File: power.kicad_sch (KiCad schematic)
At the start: 33 parts, among them J17 Conn_02x08_Odd_Even, J18 Conn_Coaxial, U11 TLV1117-33

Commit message: redoing file add
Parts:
- renumbered C31 to C42, C32 to C43, C33 to C44, C34 to C45, C35 to C46, C36 to C47, C37 to C48, C38 to C49, C39 to C50, C40 to C51, C41 to C52, C42 to C53, C43 to C54, C44 to C55, C45 to C56, C46 to C57, C47 to C58, C48 to C59, C49 to C60, C50 to C61, C51 to C62, C52 to C63, C53 to C64, C54 to C65, J17 to J18, J18 to J19, R52 to R56, R53 to R57, U11 to U12

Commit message: WIP layout
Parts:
- removed C51, C52, C57, C58: C_Polarized_Small, Capacitor_THT:CP_Radial_D8.0mm_P3.50mm, symbol Device:C_Polarized_Small
- removed C53, C54, C55, C56, C60, C61, C63, C64: C_Small, Capacitor_SMD:C_0603_1608Metric, symbol Device:C_Small
- removed L3, L4: L_Ferrite_Small, Inductor_SMD:L_0603_1608Metric, symbol Device:L_Ferrite_Small
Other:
- moved on the sheet: J18

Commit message: WIP layout
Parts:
- J18: footprint Connector_PinHeader_2.54mm:PinHeader_2x08_P2.54mm_Vertical -> Connector_PinSocket_2.54mm:PinSocket_2x08_P2.54mm_Vertical
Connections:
- net +3.3V renamed VDD
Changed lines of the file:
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@@
 			"AAAAAAAAAAAAAAAAAAAAAAAAAAAAAAAAAAAAAAAAAAAAAAAAAAAAAAAAAAAAAAAAAAAAAAAAAAAA"
 			"AAAAAAAAAAAAAAAAAAAAAAAAAAAAAAAAAAAAAAAAAAAAAAAAAAAAAAAAAAAAAAAAAAAAAAAAAAAA"
-			"AAAAAAAAAAAAAAAAAAAAAAAAAAAAAAAAAAAAAAAAAAAAAAAAAAAAAA=="
+			"AAAAAAAAAAAAAAAAAAAAAAAAAAAAAAAAAAAAAAAAAAAAAAAAAAAAAN1Ov5bOFj9lap+6KWdivzr6"
+			"7j4jJ746oHVlv4gE4z5OfZi6kRgxQa2W6sBeFIk+8KYwQUn/68C5bEc/N5MwQWlK7MBeFIk+llha"
+			"vwilBT+te666AAAAAAAAAAAAAAAAAAAAAAAAAAAAAAAA////////////////GbEcv6iSzDpU5XhB"
+			"AAAAAHpb+j8AAAAAT2eWwXYxz787XwAA8AAAAAAAAAAgAAAAAAAAAPtw4o8+XwAAsLVVfDtfAAAA"
+			"AAAAAAAAAHFvGAAAAAAAkCZufDtfAAAgGz8E/HkAAAAAAAAAAAAAAAAAAAAAAADWWDtBDcjuwHT7"
+			"BT8FAAAA4KHvc/t5AADAYO94O18AAAAAAADoino/GUxSPpqzFrtnQn0/RGsVPieJDjveIXM/okeg"
+			"PjnBCDt0ZjtBPRLvwF4UiT5rdjtBCL/vwLlsRz9BOztBEtHtwLlsRz+79Hg/l4xuPkj+DzsAAAAA"
+			"AAAAAAAAAAAAAAAAAAAAAAAAAAD///////////////96THU+RhEUO3PGHkEAAAAAk8eiP6mshMGp"
+			"rIRBzycvPztfAADwAAAAAAAAACAAAAAAAAAA63Pijz5fAADAtlV8O18AAAAAAAAAAAAAYW4YAAAA"
+			"AACQJm58O18AACAbPwT8eQAAAAAAAAAAAAAAAAAAAAAAACp1MEEu6OzAdPsFPwUAAADgoe9z+3kA"
+			"AMBg73g7XwAAAAAAAKJ1Zb+GBOM+TX2YuilnYr86+u4+Iye+Ot4vc7/38p8+HNbQOjeTMEFpSuzA"
+			"XhSJPvCmMEFJ/+vAuWxHP2VDMEES0e3AuWxHPxpma793Osk+uxXTOgAAAAAAAAAAAAAAAAAAAAAA"
+			"AAAAAAAAAP///////////////8/W2r7mjuW6tRBjQQAAAABe+tE/N7OMQTezjMFxhKE+O18AAPAA"
+			"AAAAAAAAIAAAAAAAAACbcuKPPl8AANC3VXw7XwAAAAAAAAAAAABRbRgAAAAAAJAmbnw7XwAAIBs/"
+			"BPx5AAAAAAAAAAAAAAAAAAAAAAAAFm0xQSrW6cB0+wU/BQAAAOCh73P7eQAAwGDveDtfAAAAAAAA"
+			"wVcyvxaoNz81BaW6v+NKv0UdHD9ApK86dt1Ov5bOFj9lap+6msExQacV6cBeFIk+7DExQfFU6sC5"
+			"bEc/kRgxQa2W6sBeFIk+SV5Av8PoKD8UyKS6AAAAAAAAAAAAAAAAAAAAAAAAAAAAAAAA////////"
+			"////////+Mdgv8FJ2zr4C4xBAAAAAHtb+j8AAAAAiDaqwUGdz787XwAA8AAAAAAAAAAgAAAAAAAA"
+			"AIt94o8+XwAA4LhVfDtfAAAAAAAAAAAAAEFsGAAAAAAAkCZufDtfAA=="
 		)
 	)
@@
 			"AAAAZQAAAHoAAAA3AAAAZgAAAGgAAAB6AAAASAAAAFUAAAAzAAAAWgAAAFQAAABGAAAATQAAAFUA"
 			"AAB3AAAARAAAAEUAAABVAAAAWgAAAFUAAAAxAAAAdAAAAG0AAAA5AAAAQQAAAEUAAABsAAAAdgAA"
+			"AHoAAAA1AAAAUwAAAFUAAABrAAAAWgAAADMAAABTAAAAUAAAAFUAAABRAAAAQwAAAEsAAABFAAAA"
+			"WAAAAHgAAAAxAAAAMAAAAHcAAABCAAAAWQAAAHgAAABRAAAAcwAAAGsAAAA3AAAAaAAAAFkAAABC"
+			"AAAAawAAAFQAAABoAAAASgAAAEMAAABpAAAAVQAAAEkAAABJAAAAeAAAAHAAAABKAAAAWQAAADMA"
+			"AABpAAAAYQAAAEwAAABqAAAANAAAACsAAABOAAAAMgAAAHUAAAArAAAATgAAADUAAABYAAAAaAAA"
+			"AHgAAABIAAAAWQAAADYAAABYAAAAWgAAAHQAAABqAAAAMAAAADMAAABOAAAANQAAAGYAAABQAAAA"
+			"NQAAAHgAAABWAAAARgAAAFMAAABjAAAAUgAAAE8AAABKAAAAMwAAAGwAAABiAAAAZgAAAE4AAAAv"
+			"AAAAZgAAADIAAABuAAAAcgAAAFEAAAA2AAAAYgAAAFMAAABuAAAANwAAAEoAAABuAAAAUAAAAEYA"
+			"AAAxAAAAWgAAAFgAAABWAAAAOQAAAFEAAABKAAAAegAAAFcAAABqAAAAUwAAAE8AAAA0AAAAWQAA"
+			"AHgAAABUAAAAbgAAAHEAAABJAAAAUQAAAFIAAAA5AAAARwAAAHYAAABwAAAATQAAADEAAABZAAAA"
+			"SQAAAFgAAABuAAAAeAAAAGQAAAB2AAAAYgAAADgAAABmAAAAVwAAAGIAAAA3AAAATQAAAE8AAABQ"
+			"AAAANQAAAGYAAAAzAAAANwAAAHUAAABOAAAAOQAAAFIAAABMAAAAbAAAAC8AAABTAAAAZgAAAHYA"
+			"AABFAAAATAAAAGUAAAB2AAAAVQAAAHEAAABBAAAASQAAAGcAAABnAAAAagAAAEIAAABzAAAATgAA"
+			"AGQAAAB1AAAAMgAAAGEAAAArAAAATwAAAFgAAABmAAAAeQAAAGQAAAB1AAAAMwAAAGsAAAAwAAAA"
+			"dAAAAEgAAABBAAAATwAAAGoAAABNAAAARwAAAGYAAAB5AAAAegAAAG4AAAA1AAAARwAAAHIAAABW"
+			"AAAANQAAAFcAAABsAAAASgAAAGIAAABTAAAALwAAAHgAAAAvAAAALwAAAGIAAAAvAAAAOAAAAEcA"
+			"AAAvAAAAKwAAAGgAAABxAAAAWgAAAEQAAABuAAAAcgAAADcAAABiAAAAVgAAAGsAAABvAAAAUAAA"
+			"AEYAAABUAAAAMwAAAHYAAABzAAAAOQAAADIAAABkAAAAOQAAAG0AAABuAAAAbgAAADQAAAByAAAA"
+			"LwAAADgAAABTAAAAcwAAAGcAAABXAAAAUAAAAHoAAABKAAAAZgAAADYAAABCAAAAdgAAAGEAAABZ"
 			"AA=="
 		)
@@
 	)
 	(symbol
-		(lib_id "power:+3.3V")
-		(at 226.06 55.88 0)
-		(unit 1)
-		(exclude_from_sim no)
-		(in_bom yes)
-		(on_board yes)
-		(dnp no)
-		(fields_autoplaced yes)
-		(property "Reference" "#PWR099"
-			(at 226.06 59.69 0)
-			(effects
-				(font
-					(size 1.27 1.27)
-				)
-				(hide yes)
-			)
-		)
-		(property "Value" "+3.3V"
-			(at 226.06 51.7469 0)
-			(effects
-				(font
-					(size 1.27 1.27)
-				)
-			)
-		)
-		(property "Footprint" ""
-			(at 226.06 55.88 0)
-			(effects
-				(font
-					(size 1.27 1.27)
-				)
-				(hide yes)
-			)
-		)
-		(property "Datasheet" ""
-			(at 226.06 55.88 0)
-			(effects
-				(font
-					(size 1.27 1.27)
-				)
-				(hide yes)
-			)
-		)
-		(property "Description" "Power symbol creates a global label with name \"+3.3V\""
-			(at 226.06 55.88 0)
-			(effects
-				(font
-					(size 1.27 1.27)
-				)
-				(hide yes)
-			)
-		)
-		(pin "1"
-		)
-		(instances
-			(project ""
-				(path "/afe1fbe1-30b6-4eb7-94cf-5d2700d51271/1ed0643a-d8c6-437c-9189-4d518e5ee62a"
-					(reference "#PWR099")
-					(unit 1)
-				)
-			)
-		)
-	)
-	(symbol
 		(lib_id "power:GND")
 		(at 60.96 72.39 270)
@@
 			)
 		)
-		(property "Footprint" "Connector_PinHeader_2.54mm:PinHeader_2x08_P2.54mm_Vertical"
+		(property "Footprint" "Connector_PinSocket_2.54mm:PinSocket_2x08_P2.54mm_Vertical"
 			(at 68.58 69.85 0)
 			(effects
@@
 	)
 	(symbol
+		(lib_id "power:VDD")
+		(at 226.06 55.88 0)
+		(unit 1)
+		(exclude_from_sim no)
+		(in_bom yes)
+		(on_board yes)
+		(dnp no)
+		(fields_autoplaced yes)
+		(property "Reference" "#PWR073"
+			(at 226.06 59.69 0)
+			(effects
+				(font
+					(size 1.27 1.27)
+				)
+				(hide yes)
+			)
+		)
+		(property "Value" "VDD"
+			(at 226.06 51.7469 0)
+			(effects
+				(font
+					(size 1.27 1.27)
+				)
+			)
+		)
+		(property "Footprint" ""
+			(at 226.06 55.88 0)
+			(effects
+				(font
+					(size 1.27 1.27)
+				)
+				(hide yes)
+			)
+		)
+		(property "Datasheet" ""
+			(at 226.06 55.88 0)
+			(effects
+				(font
+					(size 1.27 1.27)
+				)
+				(hide yes)
+			)
+		)
+		(property "Description" "Power symbol creates a global label with name \"VDD\""
+			(at 226.06 55.88 0)
+			(effects
+				(font
+					(size 1.27 1.27)
+				)
+				(hide yes)
+			)
+		)
+		(pin "1"
+		)
+		(instances
+			(project "pcm3168a_euro1"
+				(path "/afe1fbe1-30b6-4eb7-94cf-5d2700d51271/1ed0643a-d8c6-437c-9189-4d518e5ee62a"
+					(reference "#PWR073")
+					(unit 1)
+				)
+			)
+		)
+	)
+	(symbol
 		(lib_id "power:GND")
 		(at 73.66 69.85 90)
@@
 		(on_board yes)
 		(dnp no)
-		(fields_autoplaced yes)
 		(property "Reference" "C42"
 			(at 132.969 41.4217 0)
@@
 		)
 		(property "Value" "C_Polarized_Small"
-			(at 132.969 43.846 0)
+			(at 114.046 49.784 0)
 			(effects
 				(font

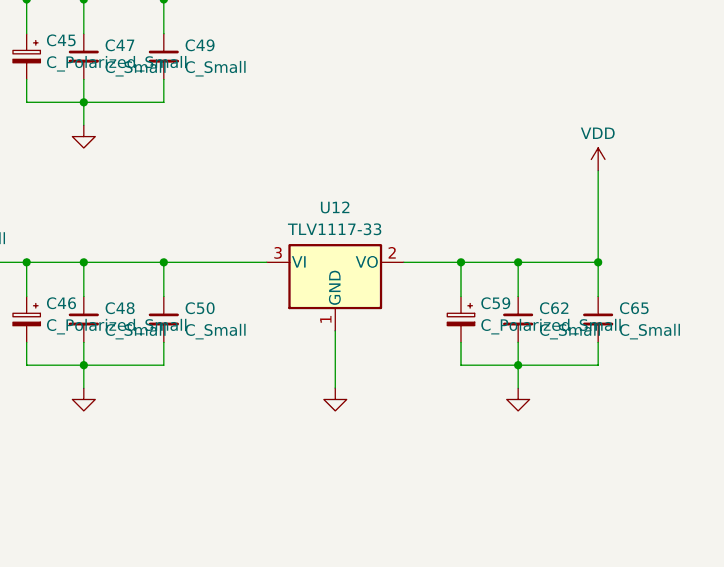
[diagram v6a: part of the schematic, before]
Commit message: WIP: layout mostly done, everything connected and looking good. still have TODO list + DRC
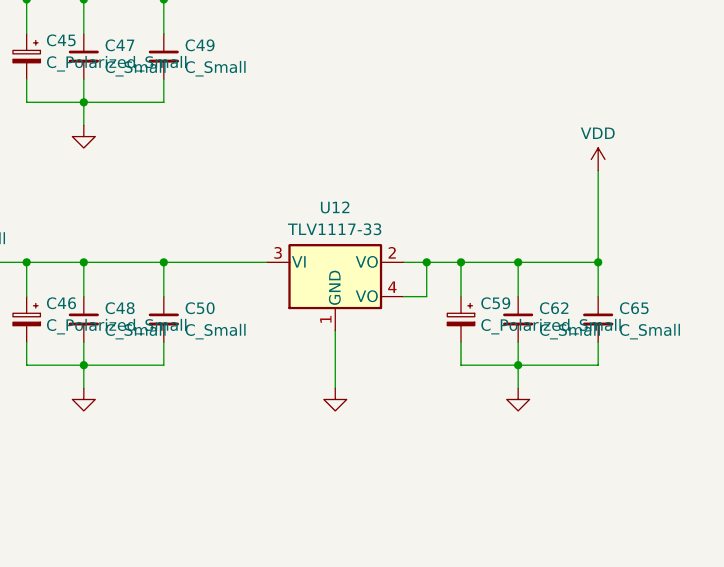
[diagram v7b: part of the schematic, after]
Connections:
- net VDD: now also U12.4 (VO)
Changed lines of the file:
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@@
 	)
 	(junction
+		(at 207.01 66.04)
+		(diameter 0)
+		(color 0 0 0 0)
+	)
+	(junction
 		(at 168.91 36.83)
 		(diameter 0)
@@
 	(wire
 		(pts
+			(xy 204.47 69.85) (xy 207.01 69.85)
+		)
+		(stroke
+			(width 0)
+			(type default)
+		)
+	)
+	(wire
+		(pts
 			(xy 146.05 48.26) (xy 146.05 45.72)
 		)
@@
 	(wire
 		(pts
+			(xy 207.01 66.04) (xy 210.82 66.04)
+		)
+		(stroke
+			(width 0)
+			(type default)
+		)
+	)
+	(wire
+		(pts
 			(xy 210.82 77.47) (xy 217.17 77.47)
 		)
@@
 	(wire
 		(pts
+			(xy 207.01 69.85) (xy 207.01 66.04)
+		)
+		(stroke
+			(width 0)
+			(type default)
+		)
+	)
+	(wire
+		(pts
 			(xy 60.96 67.31) (xy 57.15 67.31)
 		)
@@
 	(wire
 		(pts
-			(xy 204.47 66.04) (xy 210.82 66.04)
+			(xy 204.47 66.04) (xy 207.01 66.04)
 		)
 		(stroke
@@
 			"8cCa12QAAAsU50CqpavA8DJzPaXC80DgDanAa3l+PVhr7UDEWarALtZ4PQIAAACYdeDP0WQAAAAA"
 			"AAAAAAAAAAAAAAAAAACAZCrMXHAAAGTN5j4YN6o+AAAAANFkAADAAAAAAAAAAIFbAAAAAAAAkPG9"
-			"29FkAAAgG/+8XXAAAAAAAAAAAAAAAAAAAAAAAABo8cCa12QAAJ0z5g=="
+			"29FkAAAgG/+8XXAAAAAAAAAAAAAAAAAAAAAAAABo8cCa12QAAJ0z5gAAAAAAAAAAAAAAAAAAAAAA"
+			"AAAAAAAAAAAAAAAAAAAAAAAAAAAAAAAAAAAAAAAAAAAAAAAAAAAAAAAAAAAAAAAAAAAAAAAAAAAA"
+			"AAAAAAAAAAAAAAAAAAAAAAAAAAAAAAAAAAAAAAAAAAAAAAAAAAAAAAAAAAAAAAAAAAAAAAAAAAAA"
+			"AAAAAAAAAAAAAAAAAAAAAAAAAAAAAAAAAAAAAAAAAAAAAAAAAAAAAAAAAAAAAAAAAAAAAAAAAAAA"
+			"AAAAAAAAAAAAAAAAAAAAAAAAAAAAAAAAAAAAAAAAAAAAAAAAAAAAAAAAAAAAAAAAAAAAAAAAAAAA"
+			"AAAAAAAAAAAAAAAAAAAAAAAAAAAAAAAAAAAAAAAAAAAAAAAAAAAAAAAAAAAAAAAAAAAAAAAAAAAA"
+			"AAAAAAAAAAAAAAAAAAAAAAAAAAAAAAAAAAAAAAAAAAAAAAAAAAAAAAAAAAAAAAAAAAAAAAAAAAAA"
+			"AAAAAAAAAAAAAAAAAAAAAAAAAAAAAAAAAAAAAAAAAAAAAAAAAAAAAAAAAAAAAAAAAAAAAAAAAAAA"
+			"AAAAAAAAAAAAAAAAAAAAAAAAAAAAAAAAAAAAAAAAAAAAAAAAAAAAAAAAAAAAAAAAAAAAAAAAAAAA"
+			"AAAAAAAAAAAAAAAAAAAAAAAAAAAAAAAAAAAAAAAAAAAAAAAAAAAAAAAAAAAAAAAAAAAAAAAAAAAA"
+			"AAAAAAAAAAAAAAAAAAAAAAAAAAAAAAAAAAAAAAAAAAAAAAAAAAAAAAAAAAAAAAAAAAAAAAAAAAAA"
+			"AAAAAAAAAAAAAAAAAAAAAAAAAAAAAAAAAAAAAAAAAAAAAAAAAAAAAAAAAAAAAAAAAAAAAAAAAAAA"
+			"AAAAAAAAAAAAAAAAAAAAAAAAAAAAAAAAAAAAAAAAAAAAAAAAAAAAAAAAAAAAAAAAAAAAAAAAAAAA"
+			"AAAAAAAAAAAAAAAAAAAAAAAAAAAAAAAAAAAAAAAAAAAAAAAAAAAAAAAAAAAAAAAAAAAAAAAAAAAA"
+			"AAAAAAAAAAAAAAAAAAAAAAAAAAAAAAAAAAAAAAAAAAAAAAAAAAAAAAAAAAAAAAAAAAAAAAAAAAAA"
+			"AAAAAAAAAAAAAAAAAAAAAAAAAAAAAAAAAAAAAAAAAAAAAAAAAAAAAAAAAAAAAAAAAAAAAAAAAAAA"
+			"AAAAAAAAAAAAAAAAAAAAAAAAAAAAAAAAAAAAAAAAAAAAAAAAAAAAAAAAAAAAAAAAAAAAAAAAAAAA"
+			"AAAAAAAAAAAAAAAAAAAAAAAAAAAAAAAAAAAAAAAAAAAAAAAAAAAAAAAAAAAAAAAAAAAAAAAAAAAA"
+			"AAAAAAAAAAAAAAAAAAAAAAAAAAAAAAAAAAAAAAAAAAAAAAAAAAAAAA=="
 		)
 	)
@@
 			"AEMAAAA1AAAAUQAAAHQAAAA5AAAALwAAAEgAAAAzAAAANwAAAHcAAABRAAAANQAAAGkAAABiAAAA"
 			"RQAAADgAAAAyAAAAVwAAACsAAABQAAAAVwAAAC8AAABpAAAAQQAAAGQAAABiAAAAOAAAAEoAAAB2"
+			"AAAARAAAAHUAAABCAAAARAAAAFgAAAByAAAANAAAAHYAAAA3AAAAOQAAAC8AAABHAAAAZAAAADIA"
+			"AAB3AAAASgAAAEoAAAA5AAAAdgAAAHIAAAByAAAAYQAAAEgAAABrAAAAWgAAAFgAAAB6AAAAaAAA"
+			"AFAAAABUAAAAbwAAADcAAABsAAAAMQAAAG4AAAAwAAAAWgAAAGgAAAB2AAAAegAAAG8AAABHAAAA"
+			"QgAAADgAAABkAAAAawAAADcAAABrAAAANgAAAEIAAABLAAAARQAAADQAAABQAAAAQgAAAEsAAABI"
+			"AAAAaAAAAHgAAABDAAAARQAAAHEAAABGAAAAUwAAAGcAAABxAAAAMAAAAHQAAAAwAAAAZAAAAFIA"
+			"AABtAAAAWgAAADUAAABpAAAAeQAAADMAAAArAAAAcQAAAGwAAABJAAAAVgAAAGcAAAAwAAAAWgAA"
+			"AGQAAABzAAAAYwAAAFAAAAAzAAAAOQAAAEoAAABVAAAAbAAAAEQAAABTAAAAbAAAAGMAAABoAAAA"
+			"TwAAAEQAAAA3AAAAdwAAAGwAAAAxAAAAUAAAADMAAAB6AAAAdwAAAHMAAABJAAAAZAAAAG8AAAAx"
+			"AAAARgAAAHAAAABIAAAASQAAAHcAAAB0AAAAaQAAAGoAAABZAAAASwAAAGUAAAByAAAASgAAAHoA"
+			"AAA4AAAAWQAAAHAAAABLAAAARQAAAFoAAABYAAAAdwAAAC8AAABhAAAARAAAAGEAAABiAAAAcgAA"
+			"AFgAAABaAAAAYgAAADAAAAAwAAAAMwAAAEQAAABNAAAARwAAADMAAABiAAAAYgAAAHIAAABmAAAA"
+			"YgAAAGgAAAA0AAAAMwAAAEQAAABvAAAANgAAAFAAAABqAAAATQAAAEEAAAB4AAAAMAAAADMAAABk"
+			"AAAAaAAAACsAAABzAAAASgAAADMAAABMAAAANQAAAFYAAABkAAAAVwAAAFYAAABwAAAAQQAAAFUA"
+			"AABNAAAAdgAAAEoAAABVAAAAMwAAAHEAAABsAAAAcgAAAHoAAABTAAAAWAAAAGIAAABrAAAALwAA"
+			"AEsAAABKAAAARgAAAHUAAAB5AAAAUgAAAFcAAABBAAAAKwAAADkAAABJAAAAegAAAEMAAABPAAAA"
+			"bQAAAFIAAABkAAAASAAAAEUAAABZAAAAOAAAAGkAAABPAAAAVwAAAE8AAAA4AAAAQwAAAHcAAABB"
+			"AAAAaQAAAFQAAAA0AAAAbQAAAGIAAABGAAAAaAAAAHcAAAB2AAAANgAAAEcAAABIAAAAZAAAAFYA"
+			"AABvAAAAYwAAAGwAAABJAAAAeQAAAFMAAABOAAAATwAAAEQAAABpAAAARwAAAFQAAABqAAAALwAA"
 			"AA=="
 		)
@@
 		)
 		(property "Footprint" "Package_TO_SOT_SMD:SOT-223"
-			(at 196.85 66.04 0)
+			(at 195.072 57.658 0)
 			(effects
 				(font
@@
 		)
 		(property "Datasheet" "http://www.ti.com/lit/ds/symlink/tlv1117.pdf"
-			(at 196.85 66.04 0)
+			(at 197.104 54.864 0)
 			(effects
 				(font
@@
 		)
 		(property "Description" "800mA Low-Dropout Linear Regulator, 3.3V fixed output, TO-220/TO-252/TO-263/SOT-223"
-			(at 196.85 66.04 0)
+			(at 199.39 51.562 0)
 			(effects
 				(font
@@
 		(pin "3"
 		)
+		(pin "4"
+		)
 		(instances

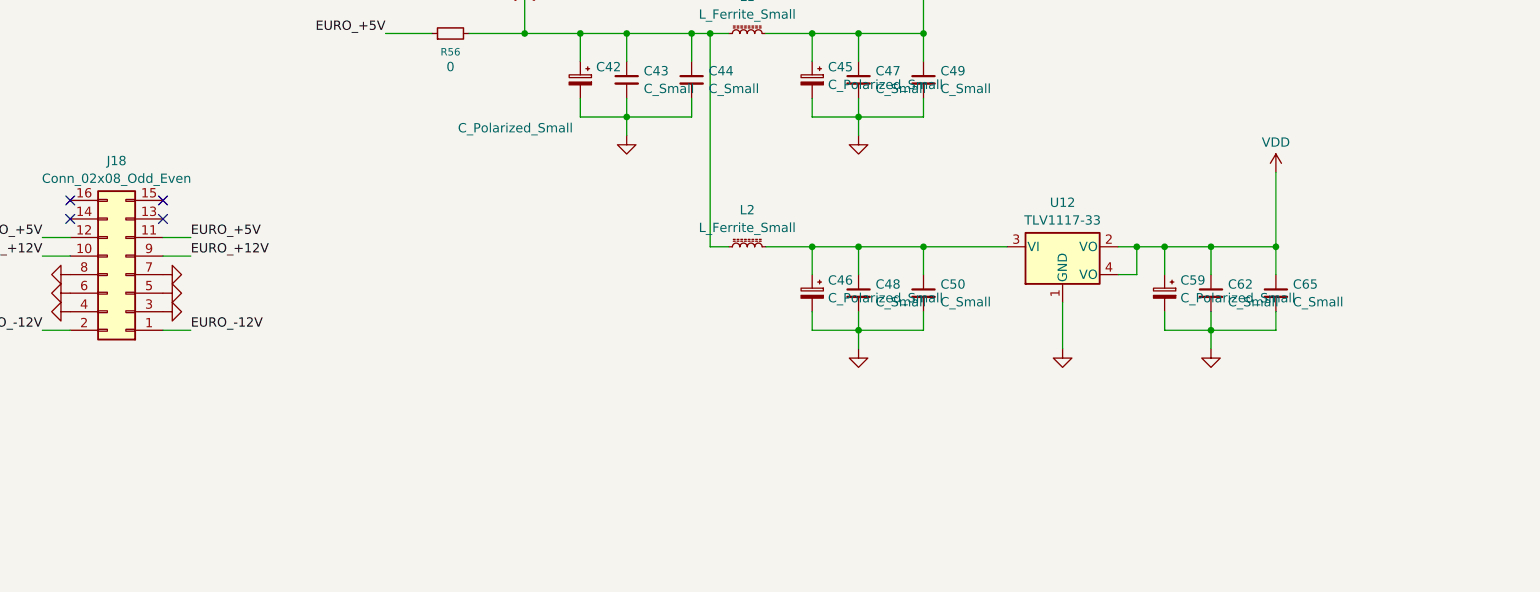
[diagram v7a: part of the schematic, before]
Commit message: WIP need to fix OPA1637 footprint
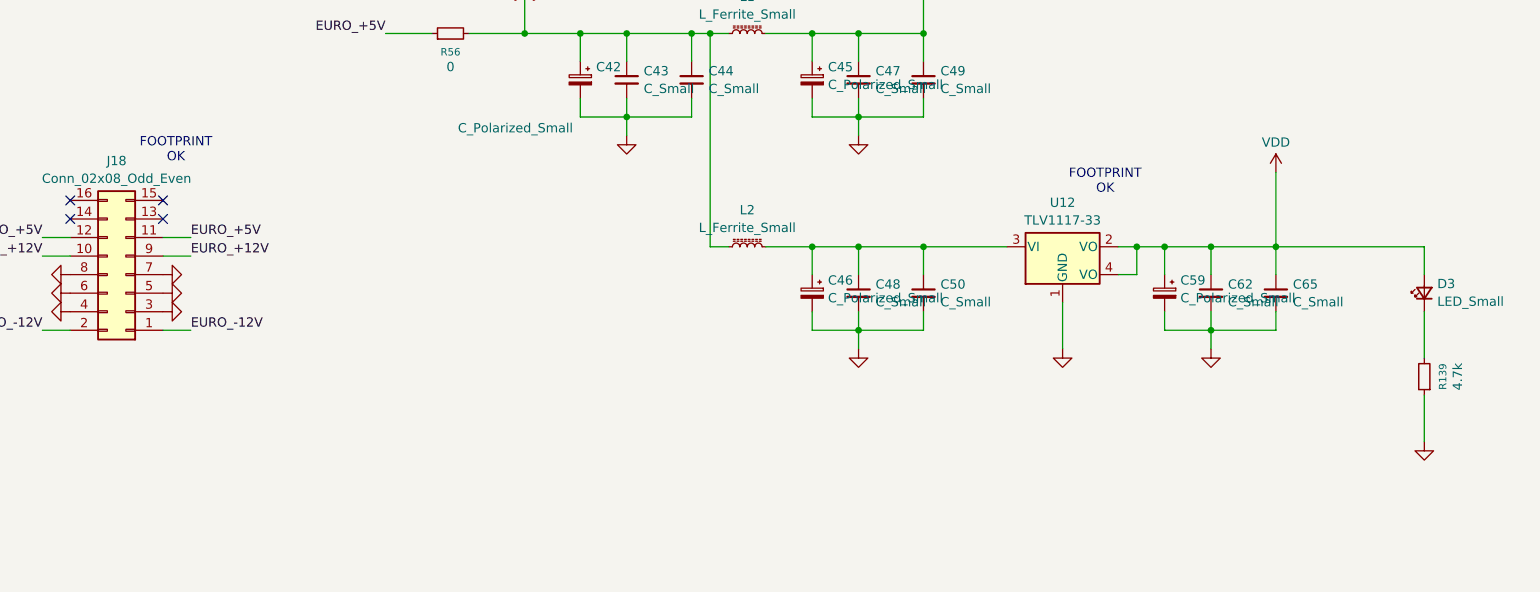
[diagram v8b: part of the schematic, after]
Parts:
- added D3: LED_Small, LED_THT:LED_D3.0mm, symbol Device:LED_Small
- added R139: 4.7k, Resistor_SMD:R_0603_1608Metric, symbol Device:R_Small
- J19: footprint Connector_Coaxial:SMA_Amphenol_901-144_Vertical -> pcm3168a_euro1:SMA_Amphenol_901-144_Vertical_awl1
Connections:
- net GND: now also R139.1
- net VDD: now also D3.2 (A)
- new net: D3.1 (K), R139.2
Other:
- note added: "FOOTPRINT OK"
